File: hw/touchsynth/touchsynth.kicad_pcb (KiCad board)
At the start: 2 copper layers, 100 x 100 mm, 245 parts, among them J1 PWR 9-12V, J2 SWIO, J3 MIDI IN, J4 LINE OUT, Q1 MMBT3904, Q10 MMBT3904, Q11 BC847BS, Q12 MMBT3904, Q13 BC847BS, Q2 2N7002, Q3 MMBT3904, Q4 BC847BS, Q5 BC847BS, Q6 BC847BS, Q7 BC847BS, Q8 BC847BS, Q9 BC847BS, U1 78L05, U10 TL072, U11 TL072, U12 LM324, U2 TL072, U3 CH32V003F4P6 / CH32V002F4P6, U4 LTV-817S, U5 CD4051B, U6 CD4051B, U7 74HC595, U8 74HC595, U9 74HC595

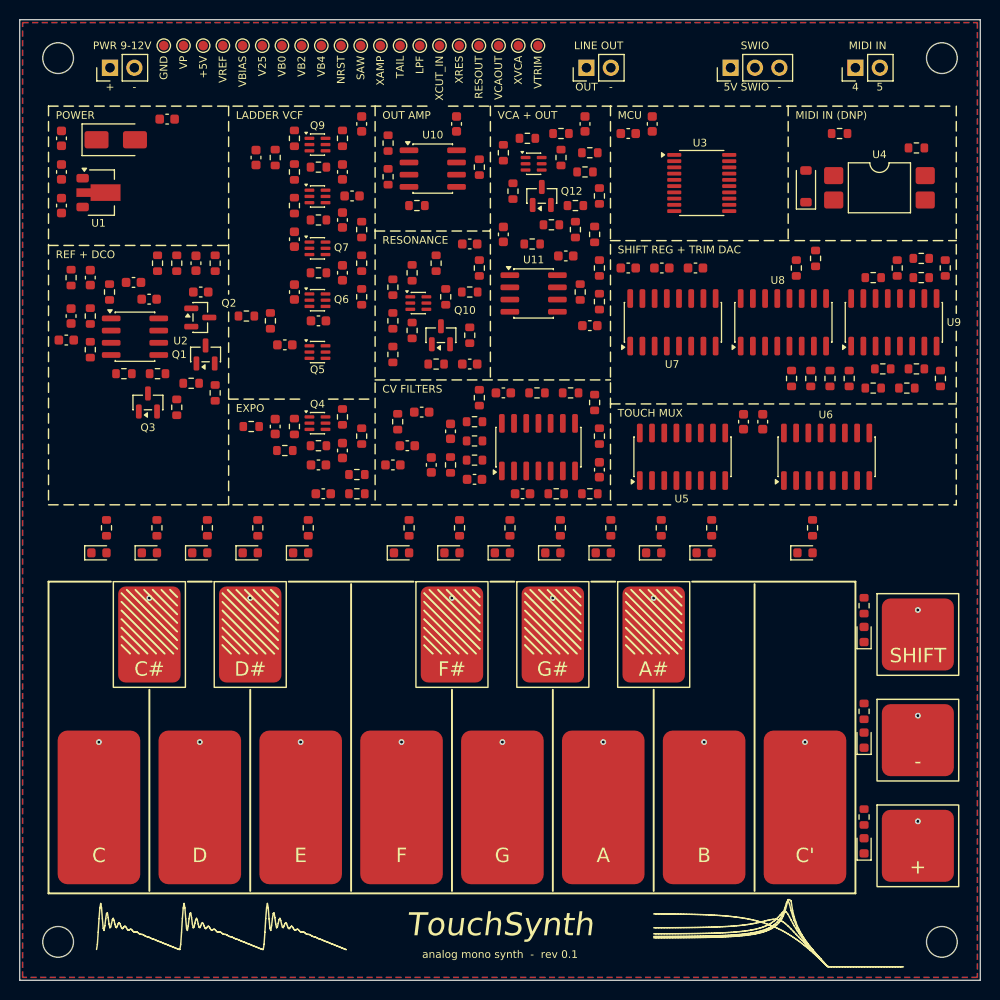
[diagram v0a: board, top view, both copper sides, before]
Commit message: 4-layer PCB: keys I/O row, trim DAC by the VCA, full routing and fab outputs
- 4 layers: F.Cu signals, In1 solid GND, In2 split power (VP analog / +5V digital / GND under the keys),
  B.Cu signals; no plane and no foreign tracks under the touch pads
- floorplan: analog blocks 72 x 36 mm in signal-flow order, right column MIDI / trim DAC / MCU,
  keys I/O row (touch muxes, LED shift registers) directly above the keys; shorter white keys,
  function pads flush with the keybed; test points inside their blocks, two THT scope-ground pins
- routing pipeline: plane stitch vias, pre-routed plane nets, Freerouting, GND via grid, island
  check, A* maze router for leftovers (pcb_maze.py), rip-up repair mode
- DRC: 0 violations, 0 unconnected, schematic parity OK; JLCPCB gerbers / BOM / CPL via fab.py
- silkscreen: back-side credits (design: cpldcpu & Claude Opus 5.5), vias kept out of the art

Co-Authored-By: Claude Opus 5.5 (1M context) <noreply@anthropic.com>
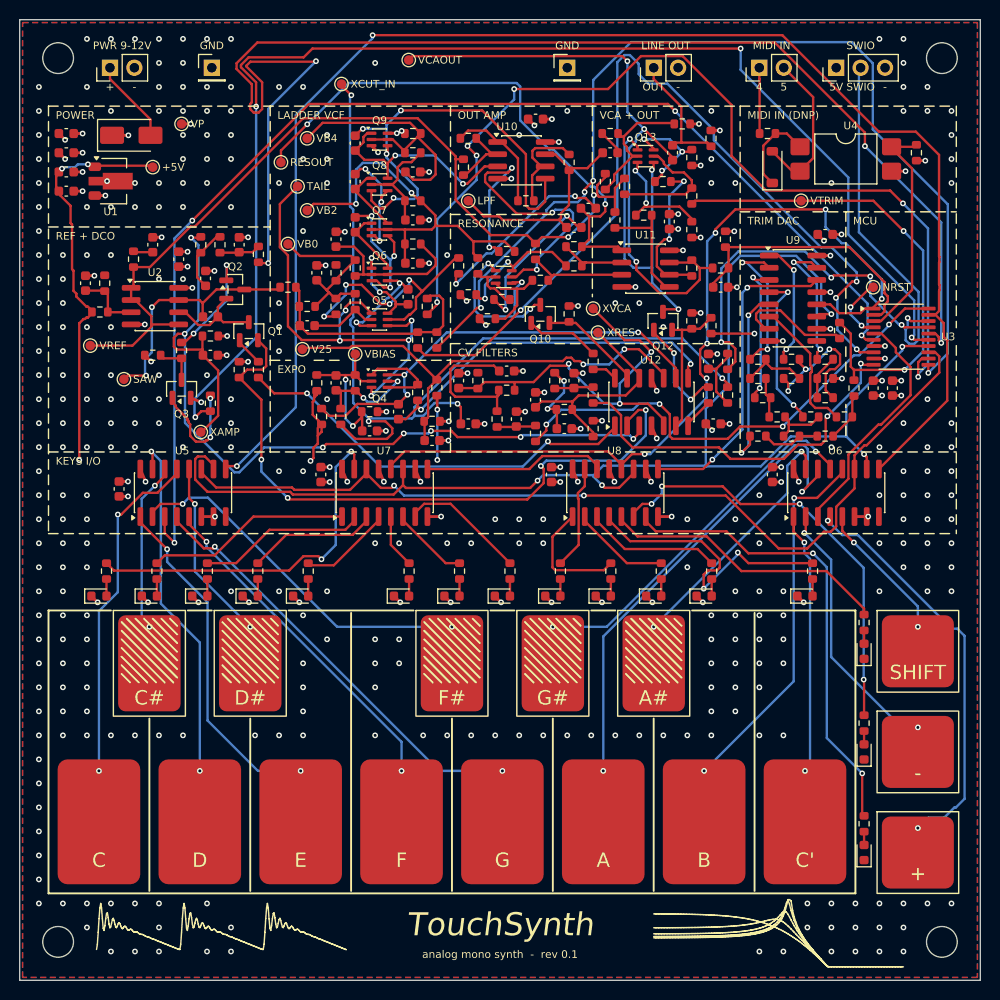
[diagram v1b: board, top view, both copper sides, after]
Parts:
- added TP21: VTRIM, TestPoint:TestPoint_Pad_D1.0mm, F.Cu at (81.3, 18.9)
- TP1: footprint TestPoint:TestPoint_Pad_D1.0mm -> Connector_PinHeader_2.54mm:PinHeader_1x01_P2.54mm_Vertical
- TP10: value NRST -> VB4
- TP11: value SAW -> NRST
- TP12: value XAMP -> SAW
- TP13: value TAIL -> XAMP
- TP14: value LPF -> TAIL
- TP15: value XCUT_IN -> LPF
- TP16: value XRES -> XCUT_IN
- TP17: value RESOUT -> XRES
- TP18: value VCAOUT -> RESOUT
- TP19: value XVCA -> VCAOUT
- TP2: value VP -> GND; footprint TestPoint:TestPoint_Pad_D1.0mm -> Connector_PinHeader_2.54mm:PinHeader_1x01_P2.54mm_Vertical
- TP20: value VTRIM -> XVCA
- TP3: value +5V -> VP
- TP4: value VREF -> +5V
- TP5: value VBIAS -> VREF
- TP6: value V25 -> VBIAS
- TP7: value VB0 -> V25
- TP8: value VB2 -> VB0
- TP9: value VB4 -> VB2
- moved C17 65.4 mm to (10.3, 48.9)
- moved TP11 59.0 mm to (88.8, 27.9)
- moved U5 52.1 mm to (17.0, 49.2)
- moved TP13 45.3 mm to (18.9, 42.9)
- moved TP12 43.8 mm to (10.8, 37.4)
- moved TP2 40.0 mm to (57.0, 5.00)
- moved C19 38.6 mm to (31.4, 47.4), turned to 90 degrees
- moved C16 37.2 mm to (90.8, 38.4)
- moved C15 36.8 mm to (88.8, 38.4), turned to 90 degrees
- moved TP5 35.0 mm to (7.35, 33.9)
- moved U7 34.9 mm to (38.0, 49.2)
- moved R58 34.5 mm to (73.7, 39.1)
- moved C48 33.6 mm to (72.2, 42.1)
- moved TP6 33.5 mm to (34.9, 34.8)
- moved C26 32.6 mm to (71.7, 35.6), turned to 90 degrees
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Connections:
- TP10 pad 1: /mcu/NRST -> VB4
- TP11 pad 1: SAW -> /mcu/NRST
- TP12 pad 1: /dco/XAMP -> SAW
- TP13 pad 1: /vcf/TAIL -> /dco/XAMP
- TP14 pad 1: LPF -> /vcf/TAIL
- TP15 pad 1: /vcf/XCUT_IN -> LPF
- TP16 pad 1: /resonance/XRES -> /vcf/XCUT_IN
- TP17 pad 1: /resonance/RESOUT -> /resonance/XRES
- TP18 pad 1: /vca/VCAOUT -> /resonance/RESOUT
- TP19 pad 1: /vca/XVCA -> /vca/VCAOUT
- TP2 pad 1: VP -> GND
- TP20 pad 1: VTRIM -> /vca/XVCA
- TP3 pad 1: +5V -> VP
- TP4 pad 1: VREF -> +5V
- TP5 pad 1: VBIAS -> VREF
- TP6 pad 1: V25 -> VBIAS
- TP7 pad 1: VB0 -> V25
- TP8 pad 1: VB2 -> VB0
- TP9 pad 1: VB4 -> VB2
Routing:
- net S2: track 0.00 -> 153.4 mm, vias 0 -> 2
- net PWM_AMP: track 0.00 -> 141.1 mm, vias 0 -> 4
- net S1_CLK: track 0.00 -> 140.9 mm, vias 0 -> 5
- net DCO_RST: track 0.00 -> 134.1 mm, vias 0 -> 4
- net TOUCH_A: track 0.00 -> 126.4 mm, vias 0 -> 4
- net SUB: track 0.00 -> 105.3 mm, vias 0 -> 4
- net PULSE: track 0.00 -> 101.7 mm, vias 0 -> 6
- net /vcf/XCUT_IN: track 0.00 -> 97.2 mm, vias 0 -> 4
- net S0_DATA: track 0.00 -> 96.3 mm, vias 0 -> 2
- net VREF: track 0.00 -> 92.5 mm, vias 0 -> 2
- net /dco/XAMP: track 0.00 -> 90.8 mm, vias 0 -> 7
- net NOISE: track 0.00 -> 90.7 mm, vias 0 -> 4
- net LATCH: track 0.00 -> 88.9 mm, vias 0 -> 6
- net +5V: track 0.00 -> 83.4 mm, vias 0 -> 24
- net GND: track 0.00 -> 77.6 mm, vias 0 -> 368
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- added copper zone on In2.Cu, net +5V
- added copper zone on In1.Cu, net GND
- added copper zone on In2.Cu, net GND
- added copper zone on In2.Cu, net VP
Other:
- copper layers 2 -> 4
- board text added: "KEYS I/O"
- board text added: "TRIM DAC"
- board text added: "rev 0.1 | 2026-09-27 | design: cpldcpu & Claude Opus 5.5"
- board text removed: "SHIFT REG + TRIM DAC"
- board text removed: "TOUCH MUX"
